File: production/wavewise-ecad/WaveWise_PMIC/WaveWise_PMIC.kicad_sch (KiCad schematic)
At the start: 19 parts, among them J1 Regulated 48V Input, J2 Panel Input, J3 Battery Direct Input, J4 24V output, J5 12V output, J6 5V output, J7 GNDs, J8 Signals output, J9 Servo output, K1 Relay_SPST-NO, Q1 2N2219

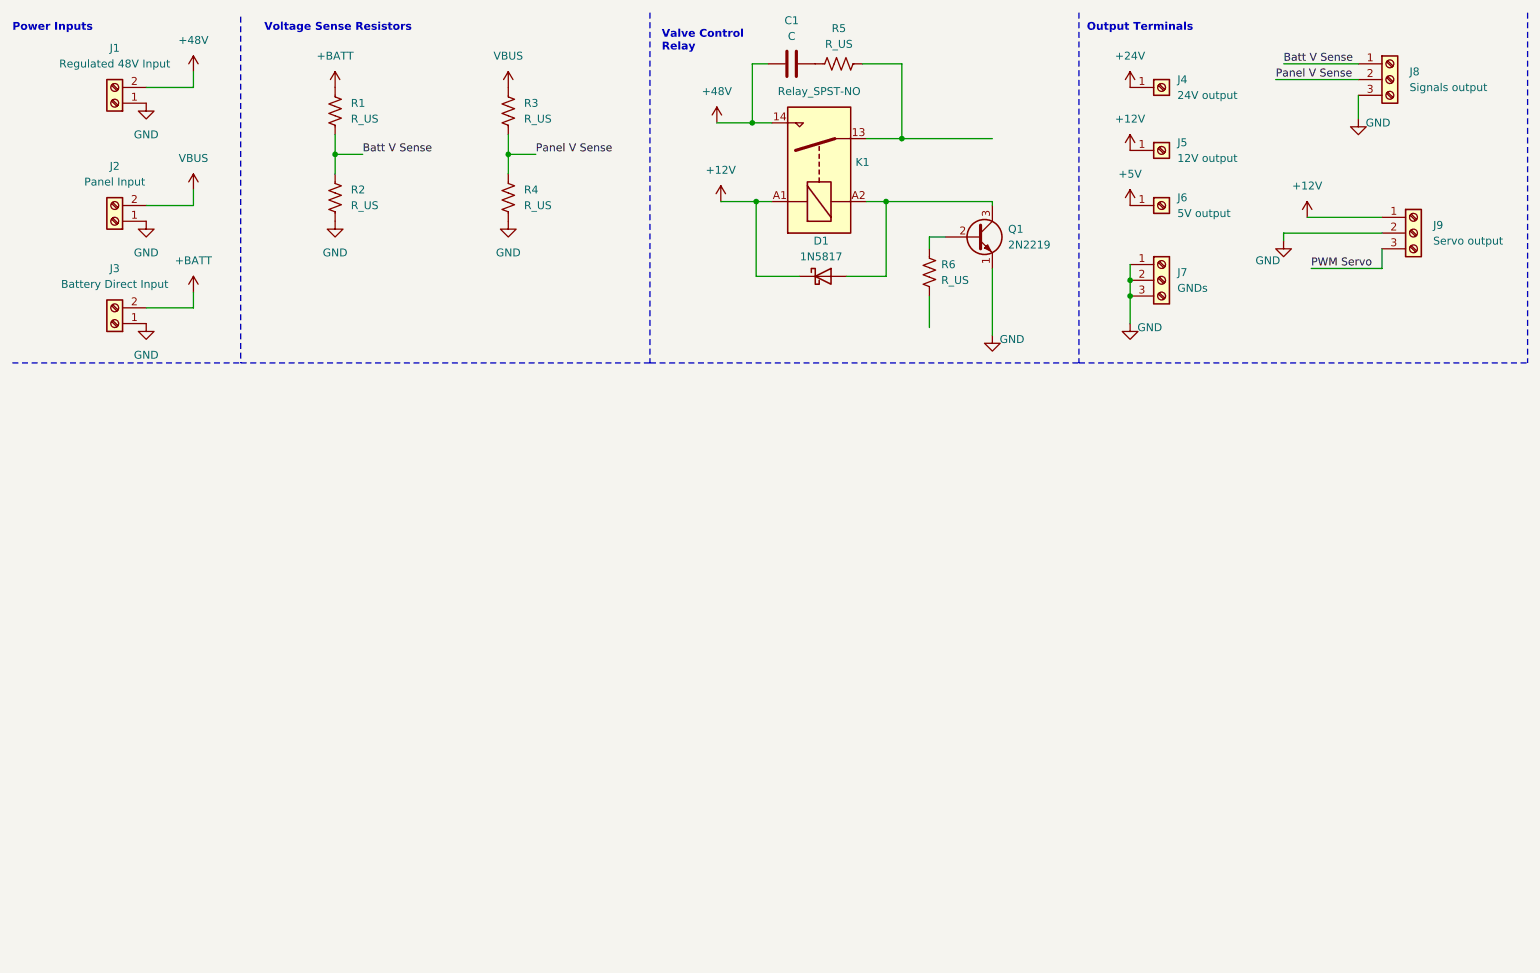
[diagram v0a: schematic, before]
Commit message: Create Hierarchical Structure to PMIC Board
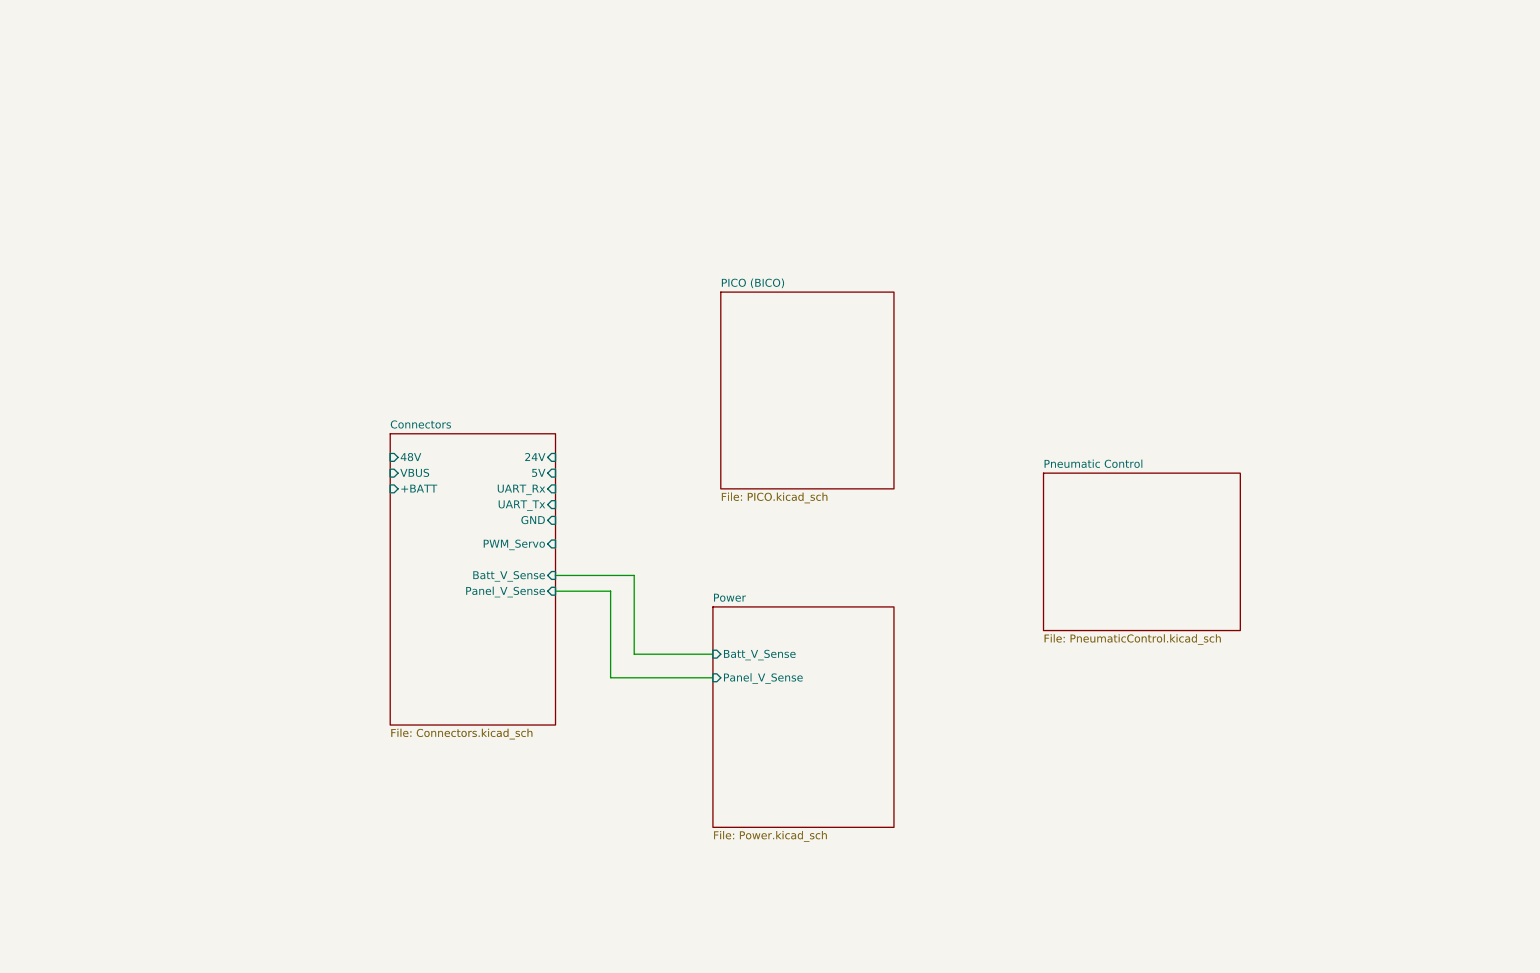
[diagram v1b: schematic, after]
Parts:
- removed C1: C, symbol Device:C
- removed D1: 1N5817, Diode_THT:D_DO-41_SOD81_P10.16mm_Horizontal, symbol Diode:1N5817
- removed J1: Regulated 48V Input, symbol Connector:Screw_Terminal_01x02
- removed J2: Panel Input, symbol Connector:Screw_Terminal_01x02
- removed J3: Battery Direct Input, symbol Connector:Screw_Terminal_01x02
- removed J4: 24V output, symbol Connector:Screw_Terminal_01x01
- removed J5: 12V output, symbol Connector:Screw_Terminal_01x01
- removed J6: 5V output, symbol Connector:Screw_Terminal_01x01
- removed J7: GNDs, symbol Connector:Screw_Terminal_01x03
- removed J8: Signals output, symbol Connector:Screw_Terminal_01x03
- removed J9: Servo output, symbol Connector:Screw_Terminal_01x03
- removed K1: Relay_SPST-NO, symbol Relay:Relay_SPST-NO
- removed Q1: 2N2219, Package_TO_SOT_THT:TO-39-3, symbol Transistor_BJT:2N2219
- removed R1, R2, R3, R4, R5, R6: R_US, symbol Device:R_US
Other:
- added sheet Connectors (Connectors.kicad_sch)
- added sheet PICO (BICO) (PICO.kicad_sch)
- added sheet Pneumatic Control (PneumaticControl.kicad_sch)
- added sheet Power (Power.kicad_sch)
- note removed: "Output Terminals"
- note removed: "Power Inputs"
- note removed: "Valve Control Relay"
- note removed: "Voltage Sense Resistors"

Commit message: add control stuff
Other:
- sheet Connectors ports: added AOUT1, AOUT2, BOUT1, BOUT2; removed none
- sheet PICO (BICO) ports: added MOSI1; removed none
- sheet Pneumatic Control ports: added -SLP, AOUT1, AOUT2, BOUT1, BOUT2, CLK, MISO1, MOSI1, SCS; removed none
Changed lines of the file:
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@@
+    (stroke (width 0) (type default))
+  )
+  (wire (pts (xy 154.94 67.564) (xy 167.386 67.564))
     (stroke (width 0) (type default))
   )
@@
     (stroke (width 0) (type default))
   )
+  (wire (pts (xy 167.386 108.966) (xy 179.07 108.966))
+    (stroke (width 0) (type default))
+  )
   (wire (pts (xy 100.33 102.87) (xy 113.03 102.87))
     (stroke (width 0) (type default))
   )
   (wire (pts (xy 113.03 115.57) (xy 125.73 115.57))
+    (stroke (width 0) (type default))
+  )
+  (wire (pts (xy 167.386 67.564) (xy 167.386 108.966))
     (stroke (width 0) (type default))
   )
@@
     (property "Sheetfile" "PICO.kicad_sch" (at 127 89.4846 0)
       (effects (font (size 1.27 1.27)) (justify left top))
+    )
+    (pin "MOSI1" input (at 154.94 67.564 0)
+      (effects (font (size 1.27 1.27)) (justify right))
     )
     (instances
@@
       (effects (font (size 1.27 1.27)) (justify left))
     )
+    (pin "AOUT1" input (at 100.33 113.284 0)
+      (effects (font (size 1.27 1.27)) (justify right))
+    )
+    (pin "BOUT2" input (at 100.33 118.618 0)
+      (effects (font (size 1.27 1.27)) (justify right))
+    )
+    (pin "BOUT1" input (at 100.33 121.158 0)
+      (effects (font (size 1.27 1.27)) (justify right))
+    )
+    (pin "AOUT2" input (at 100.33 116.078 0)
+      (effects (font (size 1.27 1.27)) (justify right))
+    )
     (instances
       (project "WaveWise_PMIC"
@@
       (effects (font (size 1.27 1.27)) (justify left top))
     )
+    (pin "AOUT1" input (at 179.07 90.932 180)
+      (effects (font (size 1.27 1.27)) (justify left))
+    )
+    (pin "AOUT2" input (at 179.07 93.726 180)
+      (effects (font (size 1.27 1.27)) (justify left))
+    )
+    (pin "BOUT1" input (at 179.07 96.266 180)
+      (effects (font (size 1.27 1.27)) (justify left))
+    )
+    (pin "BOUT2" input (at 179.07 98.806 180)
+      (effects (font (size 1.27 1.27)) (justify left))
+    )
+    (pin "MISO1" input (at 179.07 101.346 180)
+      (effects (font (size 1.27 1.27)) (justify left))
+    )
+    (pin "SCS" input (at 179.07 103.886 180)
+      (effects (font (size 1.27 1.27)) (justify left))
+    )
+    (pin "CLK" input (at 179.07 106.426 180)
+      (effects (font (size 1.27 1.27)) (justify left))
+    )
+    (pin "MOSI1" input (at 179.07 108.966 180)
+      (effects (font (size 1.27 1.27)) (justify left))
+    )
+    (pin "-SLP" input (at 210.82 90.932 0)
+      (effects (font (size 1.27 1.27)) (justify right))
+    )
     (instances

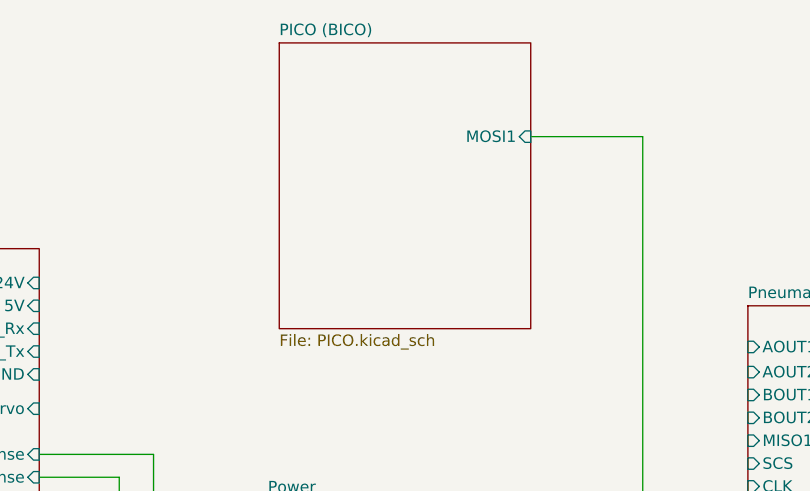
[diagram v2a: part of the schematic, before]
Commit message: Added some footprints not all yet though
Footprint addition 3/14/2024
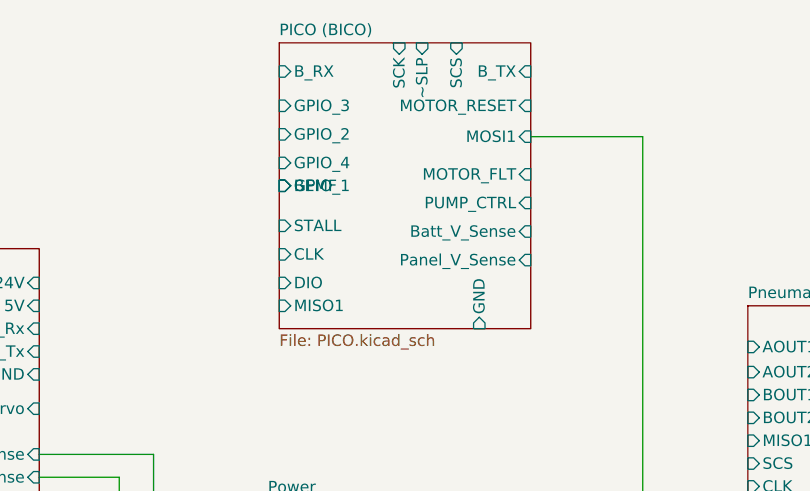
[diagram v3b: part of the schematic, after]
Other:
- sheet PICO (BICO) ports: added BEMF, B_RX, B_TX, Batt_V_Sense, CLK, DIO, GND, GPIO_1, GPIO_2, GPIO_3, GPIO_4, MISO1, MOTOR_FLT, MOTOR_RESET, PUMP_CTRL, Panel_V_Sense, SCK, SCS, STALL, ~SLP; removed none
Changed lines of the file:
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@@
+      (effects (font (size 1.27 1.27)) (justify right))
+    )
+    (pin "GPIO_3" input (at 127 64.135 180)
+      (effects (font (size 1.27 1.27)) (justify left))
+    )
+    (pin "GPIO_2" input (at 127 67.31 180)
+      (effects (font (size 1.27 1.27)) (justify left))
+    )
+    (pin "GPIO_4" input (at 127 70.485 180)
+      (effects (font (size 1.27 1.27)) (justify left))
+    )
+    (pin "BEMF" input (at 127 73.025 180)
+      (effects (font (size 1.27 1.27)) (justify left))
+    )
+    (pin "GPIO_1" input (at 127 73.025 180)
+      (effects (font (size 1.27 1.27)) (justify left))
+    )
+    (pin "STALL" input (at 127 77.47 180)
+      (effects (font (size 1.27 1.27)) (justify left))
+    )
+    (pin "CLK" input (at 127 80.645 180)
+      (effects (font (size 1.27 1.27)) (justify left))
+    )
+    (pin "DIO" input (at 127 83.82 180)
+      (effects (font (size 1.27 1.27)) (justify left))
+    )
+    (pin "GND" input (at 149.225 88.9 270)
+      (effects (font (size 1.27 1.27)) (justify left))
+    )
+    (pin "Panel_V_Sense" input (at 154.94 81.28 0)
+      (effects (font (size 1.27 1.27)) (justify right))
+    )
+    (pin "Batt_V_Sense" input (at 154.94 78.105 0)
+      (effects (font (size 1.27 1.27)) (justify right))
+    )
+    (pin "PUMP_CTRL" input (at 154.94 74.93 0)
+      (effects (font (size 1.27 1.27)) (justify right))
+    )
+    (pin "MOTOR_FLT" input (at 154.94 71.755 0)
+      (effects (font (size 1.27 1.27)) (justify right))
+    )
+    (pin "MOTOR_RESET" input (at 154.94 64.135 0)
+      (effects (font (size 1.27 1.27)) (justify right))
+    )
+    (pin "B_TX" input (at 154.94 60.325 0)
+      (effects (font (size 1.27 1.27)) (justify right))
+    )
+    (pin "B_RX" input (at 127 60.325 180)
+      (effects (font (size 1.27 1.27)) (justify left))
+    )
+    (pin "MISO1" input (at 127 86.36 180)
+      (effects (font (size 1.27 1.27)) (justify left))
+    )
+    (pin "SCS" input (at 146.685 57.15 90)
+      (effects (font (size 1.27 1.27)) (justify right))
+    )
+    (pin "~SLP" input (at 142.875 57.15 90)
+      (effects (font (size 1.27 1.27)) (justify right))
+    )
+    (pin "SCK" input (at 140.335 57.15 90)
       (effects (font (size 1.27 1.27)) (justify right))
     )

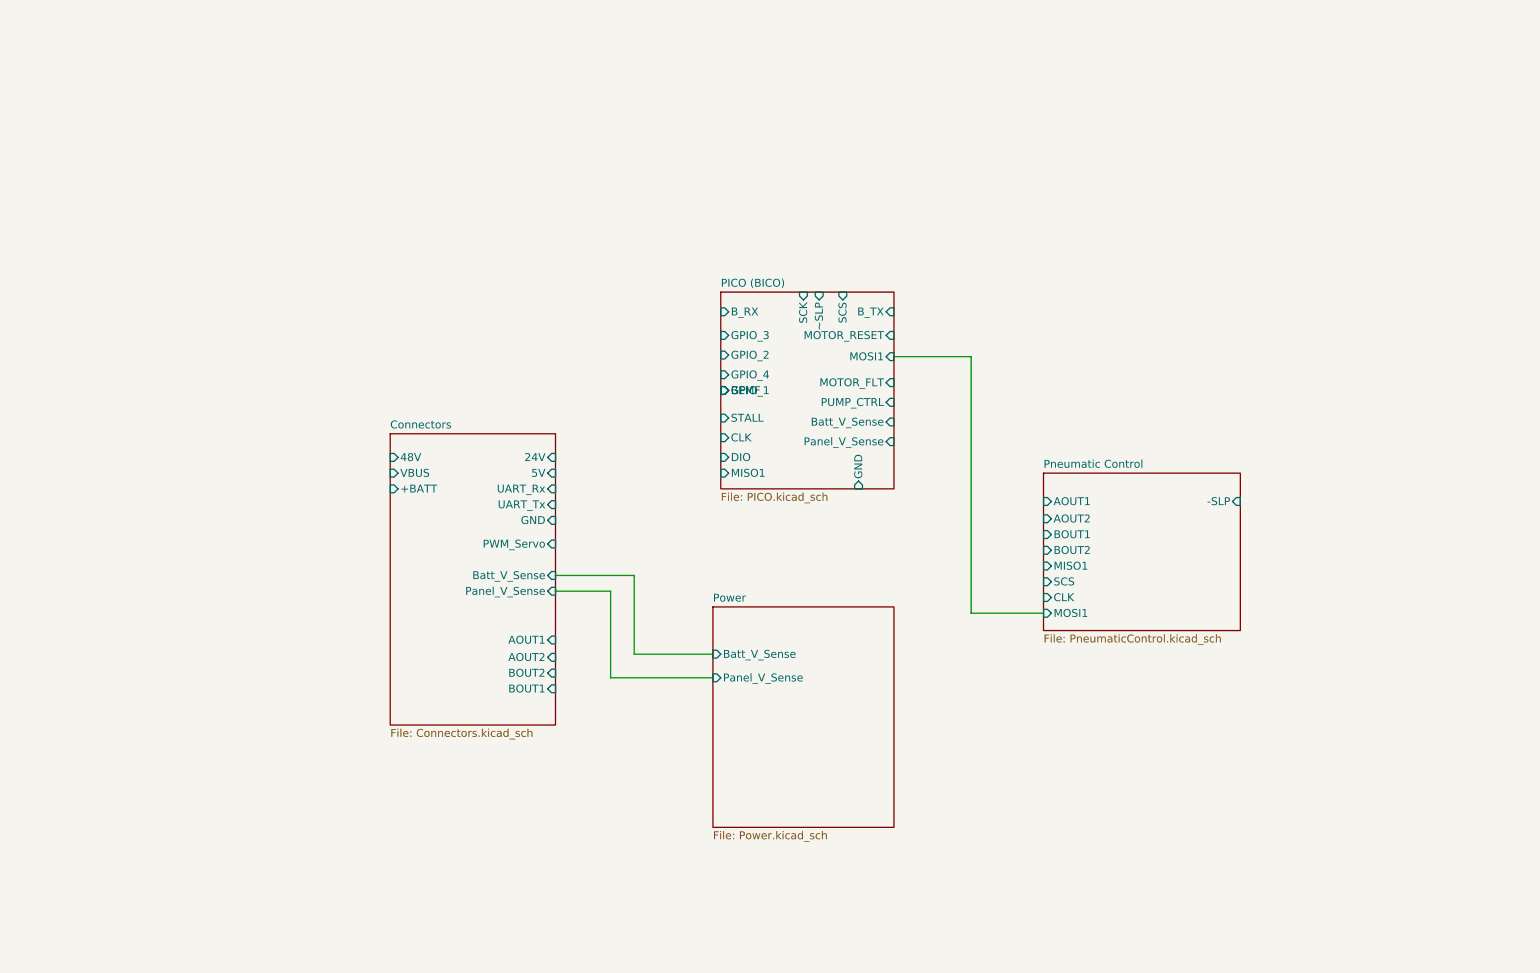
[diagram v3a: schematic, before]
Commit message: updated root and adding connectors
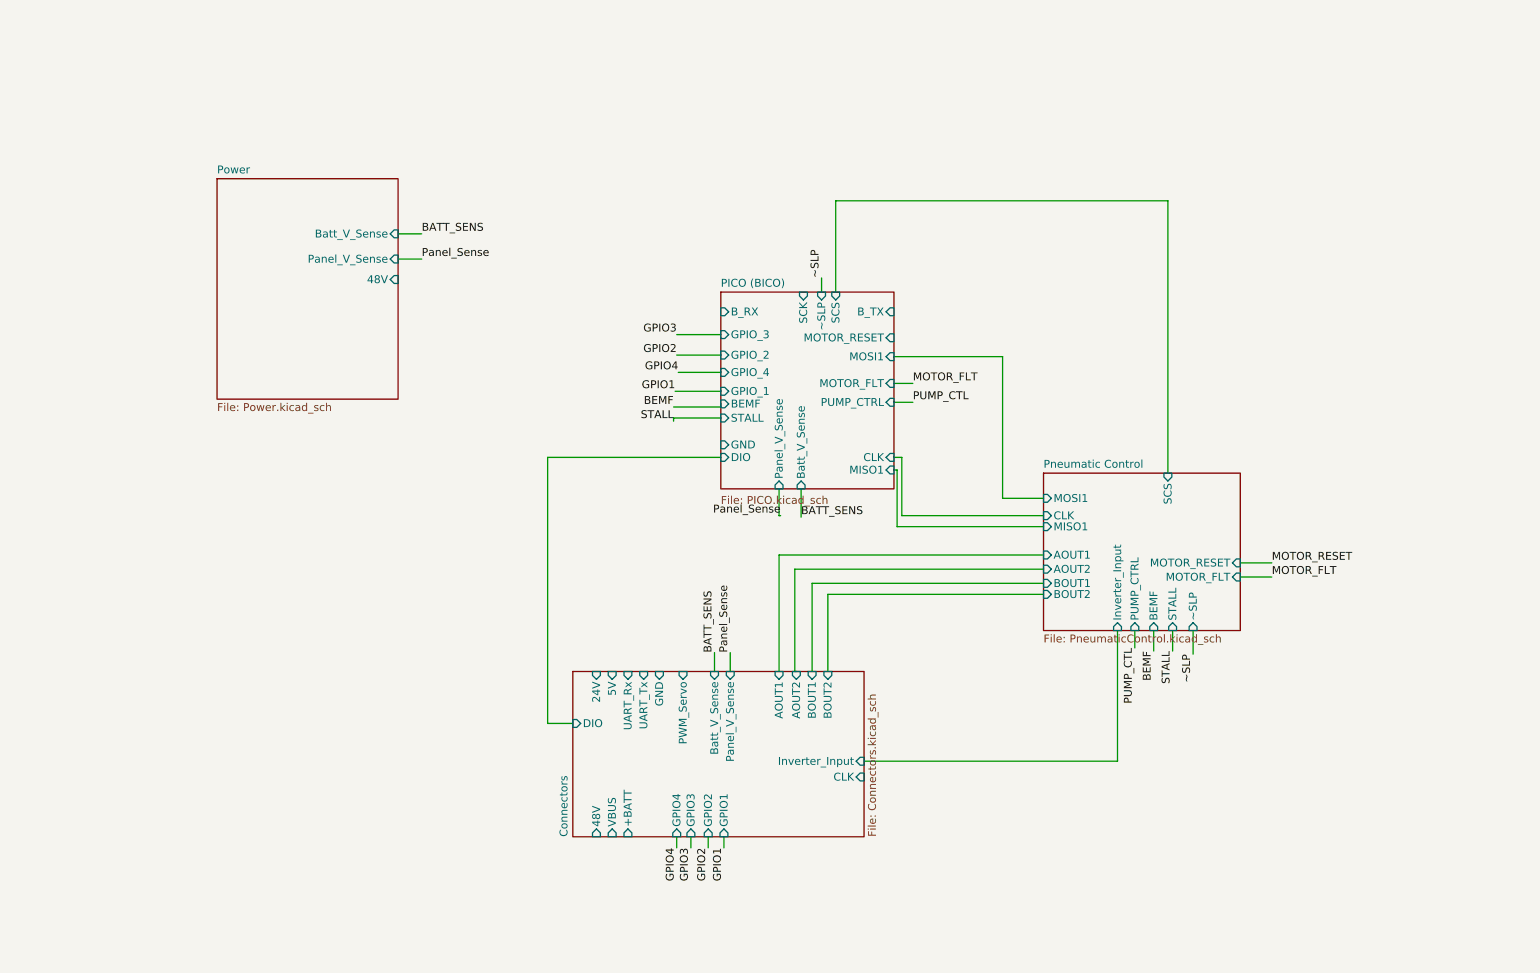
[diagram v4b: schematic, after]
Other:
- sheet Connectors ports: added CLK, DIO, GPIO1, GPIO2, GPIO3, GPIO4, Inverter_Input; removed none
- sheet Pneumatic Control ports: added BEMF, Inverter_Input, MOTOR_FLT, MOTOR_RESET, PUMP_CTRL, STALL, ~SLP; removed -SLP
- sheet Power ports: added 48V; removed none

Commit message: adding more to root page and updating for battery sensing
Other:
- sheet Connectors ports: added Batt_V_sense, Panel_V_sense, air_compDIO, dio_batt_sense, dio_panel_sense, rockblock_RX_conn, rockblock_TX_conn; removed 24V, 5V, UART_Rx, UART_Tx
- sheet PICO (BICO) ports: added GPIO4, Servo, battsensDIO, panelsensDIO; removed GPIO_4
